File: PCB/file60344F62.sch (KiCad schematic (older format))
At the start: 32 parts, among them SW1 B3F-1055, SW10 B3F-1055, SW11 B3F-1055, SW12 B3F-1055, SW13 B3F-1055, SW14 B3F-1055, SW15 B3F-1055, SW16 B3F-1055, SW2 B3F-1055, SW3 B3F-1055, SW4 B3F-1055, SW5 B3F-1055, SW6 B3F-1055, SW7 B3F-1055, SW8 B3F-1055, SW9 B3F-1055

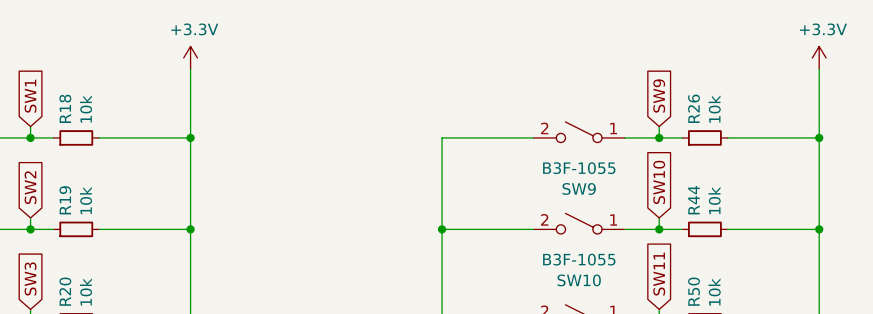
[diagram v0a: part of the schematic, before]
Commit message: Cleaned up repository. Created a BOM in iBOM Format.
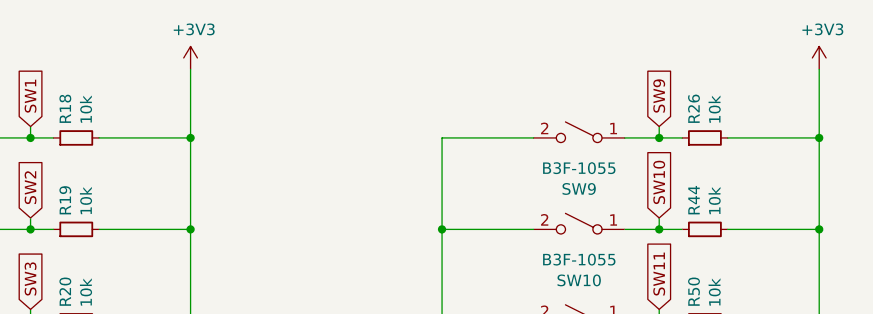
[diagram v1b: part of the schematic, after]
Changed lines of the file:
@@
 	1850 5250 1850 4750
 Connection ~ 1850 4750
-$Comp
-L power:+3.3V #PWR0163
-U 1 1 60971D53
-P 3500 1650
-F 0 "#PWR0163" H 3500 1500 50  0001 C CNN
-F 1 "+3.3V" H 3515 1823 50  0000 C CNN
-F 2 "" H 3500 1650 50  0001 C CNN
-F 3 "" H 3500 1650 50  0001 C CNN
-	1    3500 1650
-	1    0    0    -1
-$EndComp
 Wire Wire Line
 	3500 1650 3500 1950
@@
 	0    -1   -1   0
 $EndComp
-$Comp
-L power:+3.3V #PWR0165
-U 1 1 60997AA8
+Wire Wire Line
+	6250 1650 6250 1950
+Wire Wire Line
+	6250 4750 5850 4750
+Wire Wire Line
+	5850 4350 6250 4350
+Connection ~ 6250 4350
+Wire Wire Line
+	6250 4350 6250 4750
+Wire Wire Line
+	5850 3950 6250 3950
+Wire Wire Line
+	5850 3550 6250 3550
+Wire Wire Line
+	5850 3150 6250 3150
+Wire Wire Line
+	5850 2750 6250 2750
+Wire Wire Line
+	5850 2350 6250 2350
+Wire Wire Line
+	5850 1950 6250 1950
+Wire Wire Line
+	5400 1950 5550 1950
+Wire Wire Line
+	5400 2350 5550 2350
+Wire Wire Line
+	5400 2750 5550 2750
+Wire Wire Line
+	5400 3150 5550 3150
+Wire Wire Line
+	5400 3550 5550 3550
+Wire Wire Line
+	5400 3950 5550 3950
+Wire Wire Line
+	5400 4350 5550 4350
+Wire Wire Line
+	5400 4750 5550 4750
+Text GLabel 5550 1900 1    50   Input ~ 0
+SW9
+Wire Wire Line
+	5550 1900 5550 1950
+Text GLabel 5550 2300 1    50   Input ~ 0
+SW10
+Wire Wire Line
+	5550 2300 5550 2350
+Text GLabel 5550 2700 1    50   Input ~ 0
+SW11
+Wire Wire Line
+	5550 2700 5550 2750
+Text GLabel 5550 3100 1    50   Input ~ 0
+SW12
+Wire Wire Line
+	5550 3100 5550 3150
+Text GLabel 5550 3500 1    50   Input ~ 0
+SW13
+Wire Wire Line
+	5550 3500 5550 3550
+Text GLabel 5550 3900 1    50   Input ~ 0
+SW14
+Wire Wire Line
+	5550 3900 5550 3950
+Text GLabel 5550 4300 1    50   Input ~ 0
+SW15
+Wire Wire Line
+	5550 4300 5550 4350
+Text GLabel 5550 4700 1    50   Input ~ 0
+SW16
+Wire Wire Line
+	5550 4700 5550 4750
+Connection ~ 3500 1950
+Wire Wire Line
+	3500 1950 3500 2350
+Connection ~ 3500 2350
+Wire Wire Line
+	3500 2350 3500 2750
+Connection ~ 3500 2750
+Wire Wire Line
+	3500 2750 3500 3150
+Connection ~ 3500 3150
+Wire Wire Line
+	3500 3150 3500 3550
+Connection ~ 3500 3550
+Wire Wire Line
+	3500 3550 3500 3950
+Connection ~ 3500 3950
+Wire Wire Line
+	3500 3950 3500 4350
+Connection ~ 6250 3950
+Wire Wire Line
+	6250 3950 6250 4350
+Connection ~ 6250 3550
+Wire Wire Line
+	6250 3550 6250 3950
+Connection ~ 6250 3150
+Wire Wire Line
+	6250 3150 6250 3550
+Connection ~ 6250 2750
+Wire Wire Line
+	6250 2750 6250 3150
+Connection ~ 6250 2350
+Wire Wire Line
+	6250 2350 6250 2750
+Connection ~ 6250 1950
+Wire Wire Line
+	6250 1950 6250 2350
+Connection ~ 5550 1950
+Wire Wire Line
+	5550 1950 5650 1950
+Connection ~ 5550 2350
+Wire Wire Line
+	5550 2350 5650 2350
+Connection ~ 5550 2750
+Wire Wire Line
+	5550 2750 5650 2750
+Connection ~ 5550 3150
+Wire Wire Line
+	5550 3150 5650 3150
+Connection ~ 5550 3550
+Wire Wire Line
+	5550 3550 5650 3550
+Connection ~ 5550 3950
+Wire Wire Line
+	5550 3950 5650 3950
+Connection ~ 5550 4750
+Wire Wire Line
+	5550 4750 5650 4750
+Connection ~ 5550 4350
+Wire Wire Line
+	5550 4350 5650 4350
+Connection ~ 2800 4750
+Wire Wire Line
+	2800 4750 2900 4750
+Connection ~ 2800 4350
+Wire Wire Line
+	2800 4350 2900 4350
+Connection ~ 2800 3950
+Wire Wire Line
+	2800 3950 2900 3950
+Connection ~ 2800 3550
+Wire Wire Line
+	2800 3550 2900 3550
+Connection ~ 2800 3150
+Wire Wire Line
+	2800 3150 2900 3150
+Connection ~ 2800 2750
+Wire Wire Line
+	2800 2750 2900 2750
+Connection ~ 2800 2350
+Wire Wire Line
+	2800 2350 2900 2350
+Connection ~ 2800 1950
+Wire Wire Line
+	2800 1950 2900 1950
+$Comp
+L power:+3V3 #PWR0151
+U 1 1 603B74A9
 P 6250 1650
-F 0 "#PWR0165" H 6250 1500 50  0001 C CNN
-F 1 "+3.3V" H 6265 1823 50  0000 C CNN
+F 0 "#PWR0151" H 6250 1500 50  0001 C CNN
+F 1 "+3V3" H 6265 1823 50  0000 C CNN
 F 2 "" H 6250 1650 50  0001 C CNN
 F 3 "" H 6250 1650 50  0001 C CNN
@@
 	1    0    0    -1
 $EndComp
-Wire Wire Line
-	6250 1650 6250 1950
-Wire Wire Line
-	6250 4750 5850 4750
-Wire Wire Line
-	5850 4350 6250 4350
-Connection ~ 6250 4350
-Wire Wire Line
-	6250 4350 6250 4750
-Wire Wire Line
-	5850 3950 6250 3950
-Wire Wire Line
-	5850 3550 6250 3550
-Wire Wire Line
-	5850 3150 6250 3150
-Wire Wire Line
-	5850 2750 6250 2750
-Wire Wire Line
-	5850 2350 6250 2350
-Wire Wire Line
-	5850 1950 6250 1950
-Wire Wire Line
-	5400 1950 5550 1950
-Wire Wire Line
-	5400 2350 5550 2350
-Wire Wire Line
-	5400 2750 5550 2750
-Wire Wire Line
-	5400 3150 5550 3150
-Wire Wire Line
-	5400 3550 5550 3550
-Wire Wire Line
-	5400 3950 5550 3950
-Wire Wire Line
-	5400 4350 5550 4350
-Wire Wire Line
-	5400 4750 5550 4750
-Text GLabel 5550 1900 1    50   Input ~ 0
-SW9
-Wire Wire Line
-	5550 1900 5550 1950
-Text GLabel 5550 2300 1    50   Input ~ 0
-SW10
-Wire Wire Line
-	5550 2300 5550 2350
-Text GLabel 5550 2700 1    50   Input ~ 0
-SW11
-Wire Wire Line
-	5550 2700 5550 2750
-Text GLabel 5550 3100 1    50   Input ~ 0
-SW12
-Wire Wire Line
-	5550 3100 5550 3150
-Text GLabel 5550 3500 1    50   Input ~ 0
-SW13
-Wire Wire Line
-	5550 3500 5550 3550
-Text GLabel 5550 3900 1    50   Input ~ 0
-SW14
-Wire Wire Line
-	5550 3900 5550 3950
-Text GLabel 5550 4300 1    50   Input ~ 0
-SW15
-Wire Wire Line
-	5550 4300 5550 4350
-Text GLabel 5550 4700 1    50   Input ~ 0
-SW16
-Wire Wire Line
-	5550 4700 5550 4750
-Connection ~ 3500 1950
-Wire Wire Line
-	3500 1950 3500 2350
-Connection ~ 3500 2350
-Wire Wire Line
-	3500 2350 3500 2750
-Connection ~ 3500 2750
-Wire Wire Line
-	3500 2750 3500 3150
-Connection ~ 3500 3150
-Wire Wire Line
-	3500 3150 3500 3550
-Connection ~ 3500 3550
-Wire Wire Line
-	3500 3550 3500 3950
-Connection ~ 3500 3950
-Wire Wire Line
-	3500 3950 3500 4350
-Connection ~ 6250 3950
-Wire Wire Line
-	6250 3950 6250 4350
-Connection ~ 6250 3550
-Wire Wire Line
-	6250 3550 6250 3950
-Connection ~ 6250 3150
-Wire Wire Line
-	6250 3150 6250 3550
-Connection ~ 6250 2750
-Wire Wire Line
-	6250 2750 6250 3150
-Connection ~ 6250 2350
-Wire Wire Line
-	6250 2350 6250 2750
-Connection ~ 6250 1950
-Wire Wire Line
-	6250 1950 6250 2350
-Connection ~ 5550 1950
-Wire Wire Line
-	5550 1950 5650 1950
-Connection ~ 5550 2350
-Wire Wire Line
-	5550 2350 5650 2350
-Connection ~ 5550 2750
-Wire Wire Line
-	5550 2750 5650 2750
-Connection ~ 5550 3150
-Wire Wire Line
-	5550 3150 5650 3150
-Connection ~ 5550 3550
-Wire Wire Line
-	5550 3550 5650 3550
-Connection ~ 5550 3950
-Wire Wire Line
-	5550 3950 5650 3950
-Connection ~ 5550 4750
-Wire Wire Line
-	5550 4750 5650 4750
-Connection ~ 5550 4350
-Wire Wire Line
-	5550 4350 5650 4350
-Connection ~ 2800 4750
-Wire Wire Line
-	2800 4750 2900 4750
-Connection ~ 2800 4350
-Wire Wire Line
-	2800 4350 2900 4350
-Connection ~ 2800 3950
-Wire Wire Line
-	2800 3950 2900 3950
-Connection ~ 2800 3550
-Wire Wire Line
-	2800 3550 2900 3550
-Connection ~ 2800 3150
-Wire Wire Line
-	2800 3150 2900 3150
-Connection ~ 2800 2750
-Wire Wire Line
-	2800 2750 2900 2750
-Connection ~ 2800 2350
-Wire Wire Line
-	2800 2350 2900 2350
-Connection ~ 2800 1950
-Wire Wire Line
-	2800 1950 2900 1950
+$Comp
+L power:+3V3 #PWR0155
+U 1 1 603B7EC7
+P 3500 1650
+F 0 "#PWR0155" H 3500 1500 50  0001 C CNN
+F 1 "+3V3" H 3515 1823 50  0000 C CNN
+F 2 "" H 3500 1650 50  0001 C CNN
+F 3 "" H 3500 1650 50  0001 C CNN
+	1    3500 1650
+	1    0    0    -1
+$EndComp
 $EndSCHEMATC

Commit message: Completed parts details on schematics and recreated gerbers and bom.
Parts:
- R18, R19, R20, R21, R22, R23, R24, R25, R26, R44, R50, R51, R52, R53, R54, R65: LCSC (none) -> C17414; Manufacturer_Name (none) -> Vishay; Manufacturer_Part_Number (none) -> CRCW080510K0FKEAC; Mouser Part Number (none) -> 71-CRCW080510K0FKEAC
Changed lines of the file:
@@
 F 2 "Resistor_SMD:R_0805_2012Metric_Pad1.15x1.40mm_HandSolder" H 3000 1950 50  0001 C CNN
 F 3 "~" H 3000 1950 50  0001 C CNN
+F 4 "C17414" H 3000 1950 50  0001 C CNN "LCSC"
+F 5 "Vishay" H 3000 1950 50  0001 C CNN "Manufacturer_Name"
+F 6 "CRCW080510K0FKEAC" H 3000 1950 50  0001 C CNN "Manufacturer_Part_Number"
+F 7 "71-CRCW080510K0FKEAC" H 3000 1950 50  0001 C CNN "Mouser Part Number"
 	1    3000 1950
 	0    -1   -1   0
@@
 F 2 "Resistor_SMD:R_0805_2012Metric_Pad1.15x1.40mm_HandSolder" H 3000 2350 50  0001 C CNN
 F 3 "~" H 3000 2350 50  0001 C CNN
+F 4 "C17414" H 3000 2350 50  0001 C CNN "LCSC"
+F 5 "Vishay" H 3000 2350 50  0001 C CNN "Manufacturer_Name"
+F 6 "CRCW080510K0FKEAC" H 3000 2350 50  0001 C CNN "Manufacturer_Part_Number"
+F 7 "71-CRCW080510K0FKEAC" H 3000 2350 50  0001 C CNN "Mouser Part Number"
 	1    3000 2350
 	0    -1   -1   0
@@
 F 2 "Resistor_SMD:R_0805_2012Metric_Pad1.15x1.40mm_HandSolder" H 3000 2750 50  0001 C CNN
 F 3 "~" H 3000 2750 50  0001 C CNN
+F 4 "C17414" H 3000 2750 50  0001 C CNN "LCSC"
+F 5 "Vishay" H 3000 2750 50  0001 C CNN "Manufacturer_Name"
+F 6 "CRCW080510K0FKEAC" H 3000 2750 50  0001 C CNN "Manufacturer_Part_Number"
+F 7 "71-CRCW080510K0FKEAC" H 3000 2750 50  0001 C CNN "Mouser Part Number"
 	1    3000 2750
 	0    -1   -1   0
@@
 F 2 "Resistor_SMD:R_0805_2012Metric_Pad1.15x1.40mm_HandSolder" H 3000 3150 50  0001 C CNN
 F 3 "~" H 3000 3150 50  0001 C CNN
+F 4 "C17414" H 3000 3150 50  0001 C CNN "LCSC"
+F 5 "Vishay" H 3000 3150 50  0001 C CNN "Manufacturer_Name"
+F 6 "CRCW080510K0FKEAC" H 3000 3150 50  0001 C CNN "Manufacturer_Part_Number"
+F 7 "71-CRCW080510K0FKEAC" H 3000 3150 50  0001 C CNN "Mouser Part Number"
 	1    3000 3150
 	0    -1   -1   0
@@
 F 2 "Resistor_SMD:R_0805_2012Metric_Pad1.15x1.40mm_HandSolder" H 3000 3550 50  0001 C CNN
 F 3 "~" H 3000 3550 50  0001 C CNN
+F 4 "C17414" H 3000 3550 50  0001 C CNN "LCSC"
+F 5 "Vishay" H 3000 3550 50  0001 C CNN "Manufacturer_Name"
+F 6 "CRCW080510K0FKEAC" H 3000 3550 50  0001 C CNN "Manufacturer_Part_Number"
+F 7 "71-CRCW080510K0FKEAC" H 3000 3550 50  0001 C CNN "Mouser Part Number"
 	1    3000 3550
 	0    -1   -1   0
@@
 F 2 "Resistor_SMD:R_0805_2012Metric_Pad1.15x1.40mm_HandSolder" H 3000 3950 50  0001 C CNN
 F 3 "~" H 3000 3950 50  0001 C CNN
+F 4 "C17414" H 3000 3950 50  0001 C CNN "LCSC"
+F 5 "Vishay" H 3000 3950 50  0001 C CNN "Manufacturer_Name"
+F 6 "CRCW080510K0FKEAC" H 3000 3950 50  0001 C CNN "Manufacturer_Part_Number"
+F 7 "71-CRCW080510K0FKEAC" H 3000 3950 50  0001 C CNN "Mouser Part Number"
 	1    3000 3950
 	0    -1   -1   0
@@
 F 2 "Resistor_SMD:R_0805_2012Metric_Pad1.15x1.40mm_HandSolder" H 3000 4350 50  0001 C CNN
 F 3 "~" H 3000 4350 50  0001 C CNN
+F 4 "C17414" H 3000 4350 50  0001 C CNN "LCSC"
+F 5 "Vishay" H 3000 4350 50  0001 C CNN "Manufacturer_Name"
+F 6 "CRCW080510K0FKEAC" H 3000 4350 50  0001 C CNN "Manufacturer_Part_Number"
+F 7 "71-CRCW080510K0FKEAC" H 3000 4350 50  0001 C CNN "Mouser Part Number"
 	1    3000 4350
 	0    -1   -1   0
@@
 F 2 "Resistor_SMD:R_0805_2012Metric_Pad1.15x1.40mm_HandSolder" H 3000 4750 50  0001 C CNN
 F 3 "~" H 3000 4750 50  0001 C CNN
+F 4 "C17414" H 3000 4750 50  0001 C CNN "LCSC"
+F 5 "Vishay" H 3000 4750 50  0001 C CNN "Manufacturer_Name"
+F 6 "CRCW080510K0FKEAC" H 3000 4750 50  0001 C CNN "Manufacturer_Part_Number"
+F 7 "71-CRCW080510K0FKEAC" H 3000 4750 50  0001 C CNN "Mouser Part Number"
 	1    3000 4750
 	0    -1   -1   0
@@
 F 2 "Resistor_SMD:R_0805_2012Metric_Pad1.15x1.40mm_HandSolder" H 5750 1950 50  0001 C CNN
 F 3 "~" H 5750 1950 50  0001 C CNN
+F 4 "C17414" H 5750 1950 50  0001 C CNN "LCSC"
+F 5 "Vishay" H 5750 1950 50  0001 C CNN "Manufacturer_Name"
+F 6 "CRCW080510K0FKEAC" H 5750 1950 50  0001 C CNN "Manufacturer_Part_Number"
+F 7 "71-CRCW080510K0FKEAC" H 5750 1950 50  0001 C CNN "Mouser Part Number"
 	1    5750 1950
 	0    -1   -1   0
@@
 F 2 "Resistor_SMD:R_0805_2012Metric_Pad1.15x1.40mm_HandSolder" H 5750 2350 50  0001 C CNN
 F 3 "~" H 5750 2350 50  0001 C CNN
+F 4 "C17414" H 5750 2350 50  0001 C CNN "LCSC"
+F 5 "Vishay" H 5750 2350 50  0001 C CNN "Manufacturer_Name"
+F 6 "CRCW080510K0FKEAC" H 5750 2350 50  0001 C CNN "Manufacturer_Part_Number"
+F 7 "71-CRCW080510K0FKEAC" H 5750 2350 50  0001 C CNN "Mouser Part Number"
 	1    5750 2350
 	0    -1   -1   0
@@
 F 2 "Resistor_SMD:R_0805_2012Metric_Pad1.15x1.40mm_HandSolder" H 5750 2750 50  0001 C CNN
 F 3 "~" H 5750 2750 50  0001 C CNN
+F 4 "C17414" H 5750 2750 50  0001 C CNN "LCSC"
+F 5 "Vishay" H 5750 2750 50  0001 C CNN "Manufacturer_Name"
+F 6 "CRCW080510K0FKEAC" H 5750 2750 50  0001 C CNN "Manufacturer_Part_Number"
+F 7 "71-CRCW080510K0FKEAC" H 5750 2750 50  0001 C CNN "Mouser Part Number"
 	1    5750 2750
 	0    -1   -1   0
@@
 F 2 "Resistor_SMD:R_0805_2012Metric_Pad1.15x1.40mm_HandSolder" H 5750 3150 50  0001 C CNN
 F 3 "~" H 5750 3150 50  0001 C CNN
+F 4 "C17414" H 5750 3150 50  0001 C CNN "LCSC"
+F 5 "Vishay" H 5750 3150 50  0001 C CNN "Manufacturer_Name"
+F 6 "CRCW080510K0FKEAC" H 5750 3150 50  0001 C CNN "Manufacturer_Part_Number"
+F 7 "71-CRCW080510K0FKEAC" H 5750 3150 50  0001 C CNN "Mouser Part Number"
 	1    5750 3150
 	0    -1   -1   0
@@
 F 2 "Resistor_SMD:R_0805_2012Metric_Pad1.15x1.40mm_HandSolder" H 5750 3550 50  0001 C CNN
 F 3 "~" H 5750 3550 50  0001 C CNN
+F 4 "C17414" H 5750 3550 50  0001 C CNN "LCSC"
+F 5 "Vishay" H 5750 3550 50  0001 C CNN "Manufacturer_Name"
+F 6 "CRCW080510K0FKEAC" H 5750 3550 50  0001 C CNN "Manufacturer_Part_Number"
+F 7 "71-CRCW080510K0FKEAC" H 5750 3550 50  0001 C CNN "Mouser Part Number"
 	1    5750 3550
 	0    -1   -1   0
@@
 F 2 "Resistor_SMD:R_0805_2012Metric_Pad1.15x1.40mm_HandSolder" H 5750 3950 50  0001 C CNN
 F 3 "~" H 5750 3950 50  0001 C CNN
+F 4 "C17414" H 5750 3950 50  0001 C CNN "LCSC"
+F 5 "Vishay" H 5750 3950 50  0001 C CNN "Manufacturer_Name"
+F 6 "CRCW080510K0FKEAC" H 5750 3950 50  0001 C CNN "Manufacturer_Part_Number"
+F 7 "71-CRCW080510K0FKEAC" H 5750 3950 50  0001 C CNN "Mouser Part Number"
 	1    5750 3950
 	0    -1   -1   0
@@
 F 2 "Resistor_SMD:R_0805_2012Metric_Pad1.15x1.40mm_HandSolder" H 5750 4350 50  0001 C CNN
 F 3 "~" H 5750 4350 50  0001 C CNN
+F 4 "C17414" H 5750 4350 50  0001 C CNN "LCSC"
+F 5 "Vishay" H 5750 4350 50  0001 C CNN "Manufacturer_Name"
+F 6 "CRCW080510K0FKEAC" H 5750 4350 50  0001 C CNN "Manufacturer_Part_Number"
+F 7 "71-CRCW080510K0FKEAC" H 5750 4350 50  0001 C CNN "Mouser Part Number"
 	1    5750 4350
 	0    -1   -1   0
@@
 F 2 "Resistor_SMD:R_0805_2012Metric_Pad1.15x1.40mm_HandSolder" H 5750 4750 50  0001 C CNN
 F 3 "~" H 5750 4750 50  0001 C CNN
+F 4 "C17414" H 5750 4750 50  0001 C CNN "LCSC"
+F 5 "Vishay" H 5750 4750 50  0001 C CNN "Manufacturer_Name"
+F 6 "CRCW080510K0FKEAC" H 5750 4750 50  0001 C CNN "Manufacturer_Part_Number"
+F 7 "71-CRCW080510K0FKEAC" H 5750 4750 50  0001 C CNN "Mouser Part Number"
 	1    5750 4750
 	0    -1   -1   0
